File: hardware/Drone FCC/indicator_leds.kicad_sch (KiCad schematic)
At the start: 48 parts, among them Q1 2N7002, Q2 2N7002, Q3 2N7002, Q4 2N7002, Q5 2N7002, Q6 2N7002, Q7 2N7002, Q8 2N7002, SW2 SW Proposito General, SW3 SW Proposito General

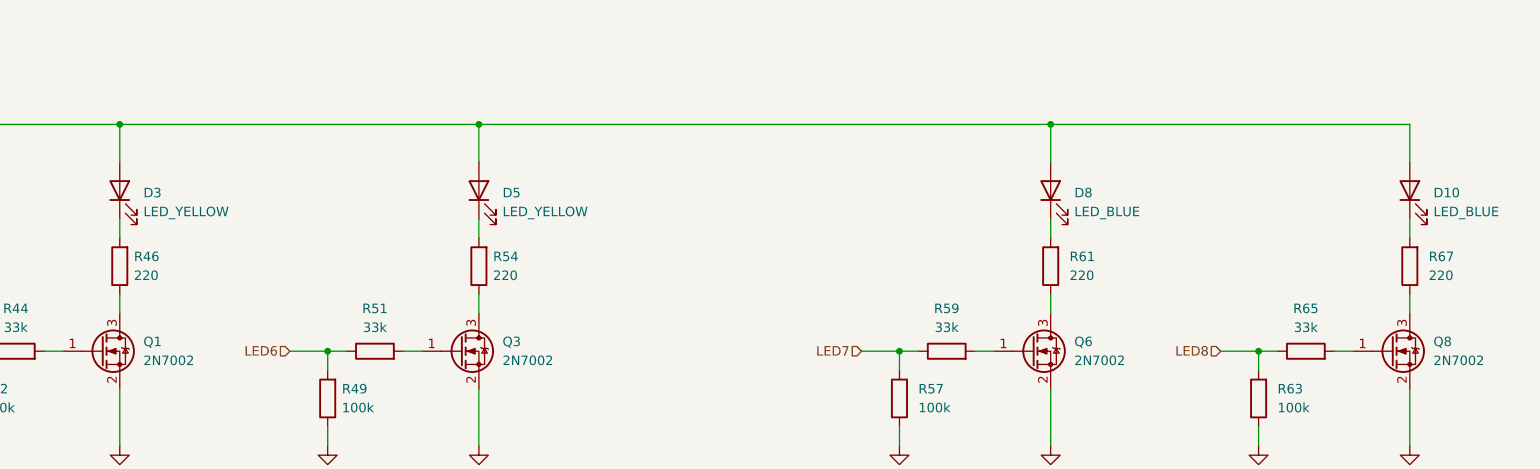
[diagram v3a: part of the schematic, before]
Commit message: moved external SPI tracks to TOP layer. Moved external I2C pull ups to TOP layer
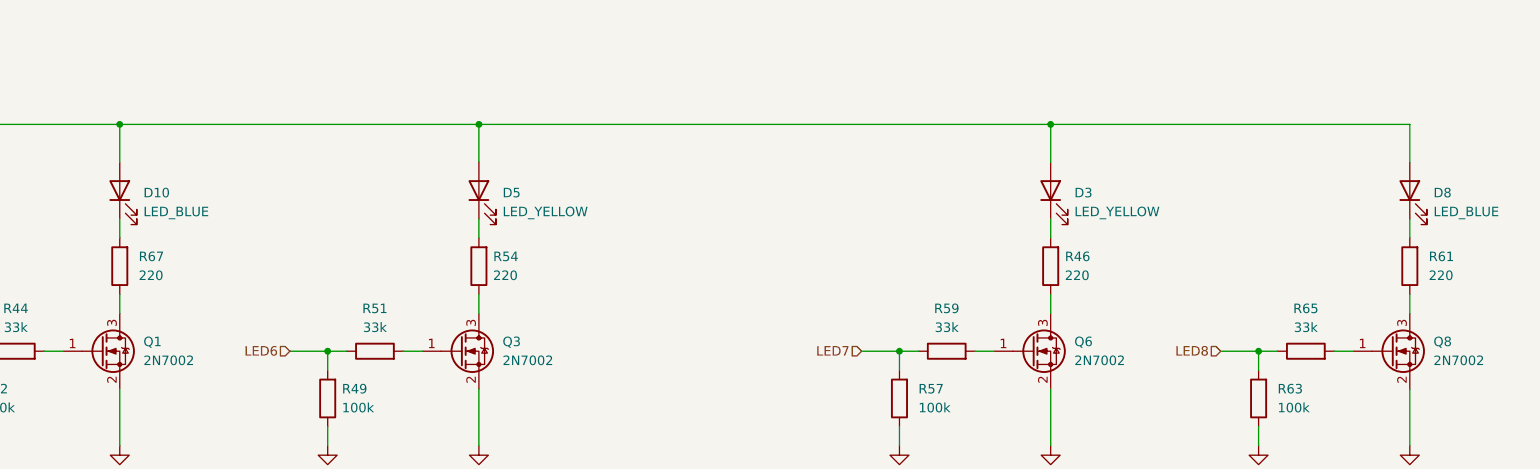
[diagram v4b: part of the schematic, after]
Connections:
- net at R46.1: now also Q6.3 (D); no longer Q1.3 (D)
- net at Q8.3 (D): now also R61.1; no longer R67.1
- new net: Q1.3 (D), R67.1
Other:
- moved on the sheet: D10, D3, D8, R46, R61, R67
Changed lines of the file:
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@@
     (pin "2")
   )
-  (symbol (lib_id "Device:R") (at 67.945 116.205 180) (unit 1)
-    (in_bom yes) (on_board yes) (fields_autoplaced)
-    (property "Reference" "R46" (id 0) (at 69.85 114.9349 0)
-      (effects (font (size 1.27 1.27)) (justify right))
-    )
-    (property "Value" "220" (id 1) (at 69.85 117.4749 0)
-      (effects (font (size 1.27 1.27)) (justify right))
-    )
-    (property "Footprint" "Resistor_SMD:R_0402_1005Metric_Pad0.72x0.64mm_HandSolder" (id 2) (at 69.723 116.205 90)
-      (effects (font (size 1.27 1.27)) hide)
-    )
-    (property "Datasheet" "~" (id 3) (at 67.945 116.205 0)
+  (symbol (lib_id "Device:R") (at 193.04 116.205 180) (unit 1)
+    (in_bom yes) (on_board yes) (fields_autoplaced)
+    (property "Reference" "R46" (id 0) (at 194.945 114.9349 0)
+      (effects (font (size 1.27 1.27)) (justify right))
+    )
+    (property "Value" "220" (id 1) (at 194.945 117.4749 0)
+      (effects (font (size 1.27 1.27)) (justify right))
+    )
+    (property "Footprint" "Resistor_SMD:R_0402_1005Metric_Pad0.72x0.64mm_HandSolder" (id 2) (at 194.818 116.205 90)
+      (effects (font (size 1.27 1.27)) hide)
+    )
+    (property "Datasheet" "~" (id 3) (at 193.04 116.205 0)
       (effects (font (size 1.27 1.27)) hide)
     )
@@
     (pin "1")
   )
-  (symbol (lib_id "Device:LED") (at 193.04 106.045 90) (unit 1)
-    (in_bom yes) (on_board yes) (fields_autoplaced)
-    (property "Reference" "D8" (id 0) (at 196.215 106.3624 90)
-      (effects (font (size 1.27 1.27)) (justify right))
-    )
-    (property "Value" "LED_BLUE" (id 1) (at 196.215 108.9024 90)
-      (effects (font (size 1.27 1.27)) (justify right))
-    )
-    (property "Footprint" "LED_SMD:LED_0805_2012Metric_Pad1.15x1.40mm_HandSolder" (id 2) (at 193.04 106.045 0)
-      (effects (font (size 1.27 1.27)) hide)
-    )
-    (property "Datasheet" "~" (id 3) (at 193.04 106.045 0)
+  (symbol (lib_id "Device:LED") (at 241.3 106.045 90) (unit 1)
+    (in_bom yes) (on_board yes) (fields_autoplaced)
+    (property "Reference" "D8" (id 0) (at 244.475 106.3624 90)
+      (effects (font (size 1.27 1.27)) (justify right))
+    )
+    (property "Value" "LED_BLUE" (id 1) (at 244.475 108.9024 90)
+      (effects (font (size 1.27 1.27)) (justify right))
+    )
+    (property "Footprint" "LED_SMD:LED_0805_2012Metric_Pad1.15x1.40mm_HandSolder" (id 2) (at 241.3 106.045 0)
+      (effects (font (size 1.27 1.27)) hide)
+    )
+    (property "Datasheet" "~" (id 3) (at 241.3 106.045 0)
       (effects (font (size 1.27 1.27)) hide)
     )
@@
     (pin "1")
   )
-  (symbol (lib_id "Device:LED") (at 67.945 106.045 90) (unit 1)
-    (in_bom yes) (on_board yes) (fields_autoplaced)
-    (property "Reference" "D3" (id 0) (at 71.12 106.3624 90)
-      (effects (font (size 1.27 1.27)) (justify right))
-    )
-    (property "Value" "LED_YELLOW" (id 1) (at 71.12 108.9024 90)
-      (effects (font (size 1.27 1.27)) (justify right))
-    )
-    (property "Footprint" "LED_SMD:LED_0805_2012Metric_Pad1.15x1.40mm_HandSolder" (id 2) (at 67.945 106.045 0)
-      (effects (font (size 1.27 1.27)) hide)
-    )
-    (property "Datasheet" "~" (id 3) (at 67.945 106.045 0)
+  (symbol (lib_id "Device:LED") (at 193.04 106.045 90) (unit 1)
+    (in_bom yes) (on_board yes) (fields_autoplaced)
+    (property "Reference" "D3" (id 0) (at 196.215 106.3624 90)
+      (effects (font (size 1.27 1.27)) (justify right))
+    )
+    (property "Value" "LED_YELLOW" (id 1) (at 196.215 108.9024 90)
+      (effects (font (size 1.27 1.27)) (justify right))
+    )
+    (property "Footprint" "LED_SMD:LED_0805_2012Metric_Pad1.15x1.40mm_HandSolder" (id 2) (at 193.04 106.045 0)
+      (effects (font (size 1.27 1.27)) hide)
+    )
+    (property "Datasheet" "~" (id 3) (at 193.04 106.045 0)
       (effects (font (size 1.27 1.27)) hide)
     )
@@
     (pin "1")
   )
-  (symbol (lib_id "Device:LED") (at 241.3 106.045 90) (unit 1)
-    (in_bom yes) (on_board yes) (fields_autoplaced)
-    (property "Reference" "D10" (id 0) (at 244.475 106.3624 90)
-      (effects (font (size 1.27 1.27)) (justify right))
-    )
-    (property "Value" "LED_BLUE" (id 1) (at 244.475 108.9024 90)
-      (effects (font (size 1.27 1.27)) (justify right))
-    )
-    (property "Footprint" "LED_SMD:LED_0805_2012Metric_Pad1.15x1.40mm_HandSolder" (id 2) (at 241.3 106.045 0)
-      (effects (font (size 1.27 1.27)) hide)
-    )
-    (property "Datasheet" "~" (id 3) (at 241.3 106.045 0)
+  (symbol (lib_id "Device:LED") (at 67.945 106.045 90) (unit 1)
+    (in_bom yes) (on_board yes) (fields_autoplaced)
+    (property "Reference" "D10" (id 0) (at 71.12 106.3624 90)
+      (effects (font (size 1.27 1.27)) (justify right))
+    )
+    (property "Value" "LED_BLUE" (id 1) (at 71.12 108.9024 90)
+      (effects (font (size 1.27 1.27)) (justify right))
+    )
+    (property "Footprint" "LED_SMD:LED_0805_2012Metric_Pad1.15x1.40mm_HandSolder" (id 2) (at 67.945 106.045 0)
+      (effects (font (size 1.27 1.27)) hide)
+    )
+    (property "Datasheet" "~" (id 3) (at 67.945 106.045 0)
       (effects (font (size 1.27 1.27)) hide)
     )
@@
     (pin "1")
   )
-  (symbol (lib_id "Device:R") (at 193.04 116.205 180) (unit 1)
-    (in_bom yes) (on_board yes) (fields_autoplaced)
-    (property "Reference" "R61" (id 0) (at 195.58 114.9349 0)
-      (effects (font (size 1.27 1.27)) (justify right))
-    )
-    (property "Value" "220" (id 1) (at 195.58 117.4749 0)
-      (effects (font (size 1.27 1.27)) (justify right))
-    )
-    (property "Footprint" "Resistor_SMD:R_0402_1005Metric_Pad0.72x0.64mm_HandSolder" (id 2) (at 194.818 116.205 90)
-      (effects (font (size 1.27 1.27)) hide)
-    )
-    (property "Datasheet" "~" (id 3) (at 193.04 116.205 0)
+  (symbol (lib_id "Device:R") (at 241.3 116.205 180) (unit 1)
+    (in_bom yes) (on_board yes) (fields_autoplaced)
+    (property "Reference" "R61" (id 0) (at 243.84 114.9349 0)
+      (effects (font (size 1.27 1.27)) (justify right))
+    )
+    (property "Value" "220" (id 1) (at 243.84 117.4749 0)
+      (effects (font (size 1.27 1.27)) (justify right))
+    )
+    (property "Footprint" "Resistor_SMD:R_0402_1005Metric_Pad0.72x0.64mm_HandSolder" (id 2) (at 243.078 116.205 90)
+      (effects (font (size 1.27 1.27)) hide)
+    )
+    (property "Datasheet" "~" (id 3) (at 241.3 116.205 0)
       (effects (font (size 1.27 1.27)) hide)
     )
@@
     (pin "1")
   )
-  (symbol (lib_id "Device:R") (at 241.3 116.205 180) (unit 1)
-    (in_bom yes) (on_board yes) (fields_autoplaced)
-    (property "Reference" "R67" (id 0) (at 243.84 114.9349 0)
-      (effects (font (size 1.27 1.27)) (justify right))
-    )
-    (property "Value" "220" (id 1) (at 243.84 117.4749 0)
-      (effects (font (size 1.27 1.27)) (justify right))
-    )
-    (property "Footprint" "Resistor_SMD:R_0402_1005Metric_Pad0.72x0.64mm_HandSolder" (id 2) (at 243.078 116.205 90)
-      (effects (font (size 1.27 1.27)) hide)
-    )
-    (property "Datasheet" "~" (id 3) (at 241.3 116.205 0)
-      (effects (font (size 1.27 1.27)) hide)
-    )
+  (symbol (lib_id "Device:R") (at 67.945 116.205 180) (unit 1)
+    (in_bom yes) (on_board yes) (fields_autoplaced)
+    (property "Reference" "R67" (id 0) (at 70.485 114.9349 0)
+      (effects (font (size 1.27 1.27)) (justify right))
+    )
+    (property "Value" "220" (id 1) (at 70.485 117.4749 0)
+      (effects (font (size 1.27 1.27)) (justify right))
+    )
+    (property "Footprint" "Resistor_SMD:R_0402_1005Metric_Pad0.72x0.64mm_HandSolder" (id 2) (at 69.723 116.205 90)
+      (effects (font (size 1.27 1.27)) hide)
+    )
+    (property "Datasheet" "~" (id 3) (at 67.945 116.205 0)
+      (effects (font (size 1.27 1.27)) hide)
+    )
